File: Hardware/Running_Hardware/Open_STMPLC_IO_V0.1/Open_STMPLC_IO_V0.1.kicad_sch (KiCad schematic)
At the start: 5 parts

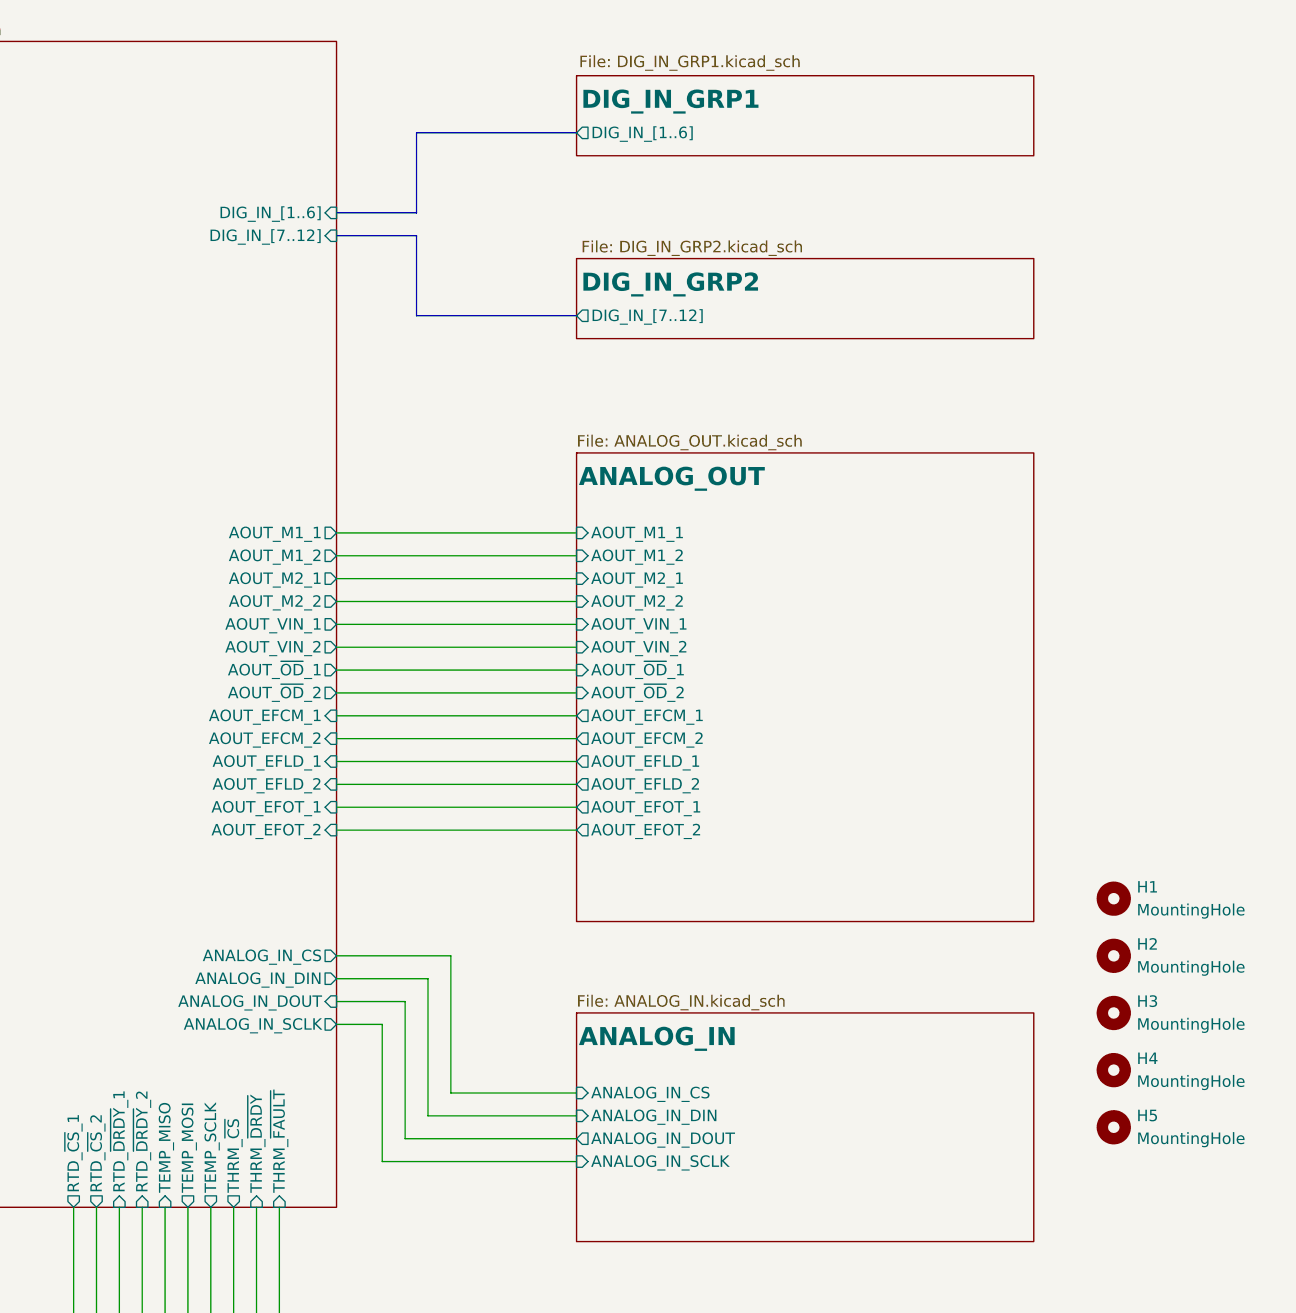
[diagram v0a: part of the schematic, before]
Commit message: Input circuit added
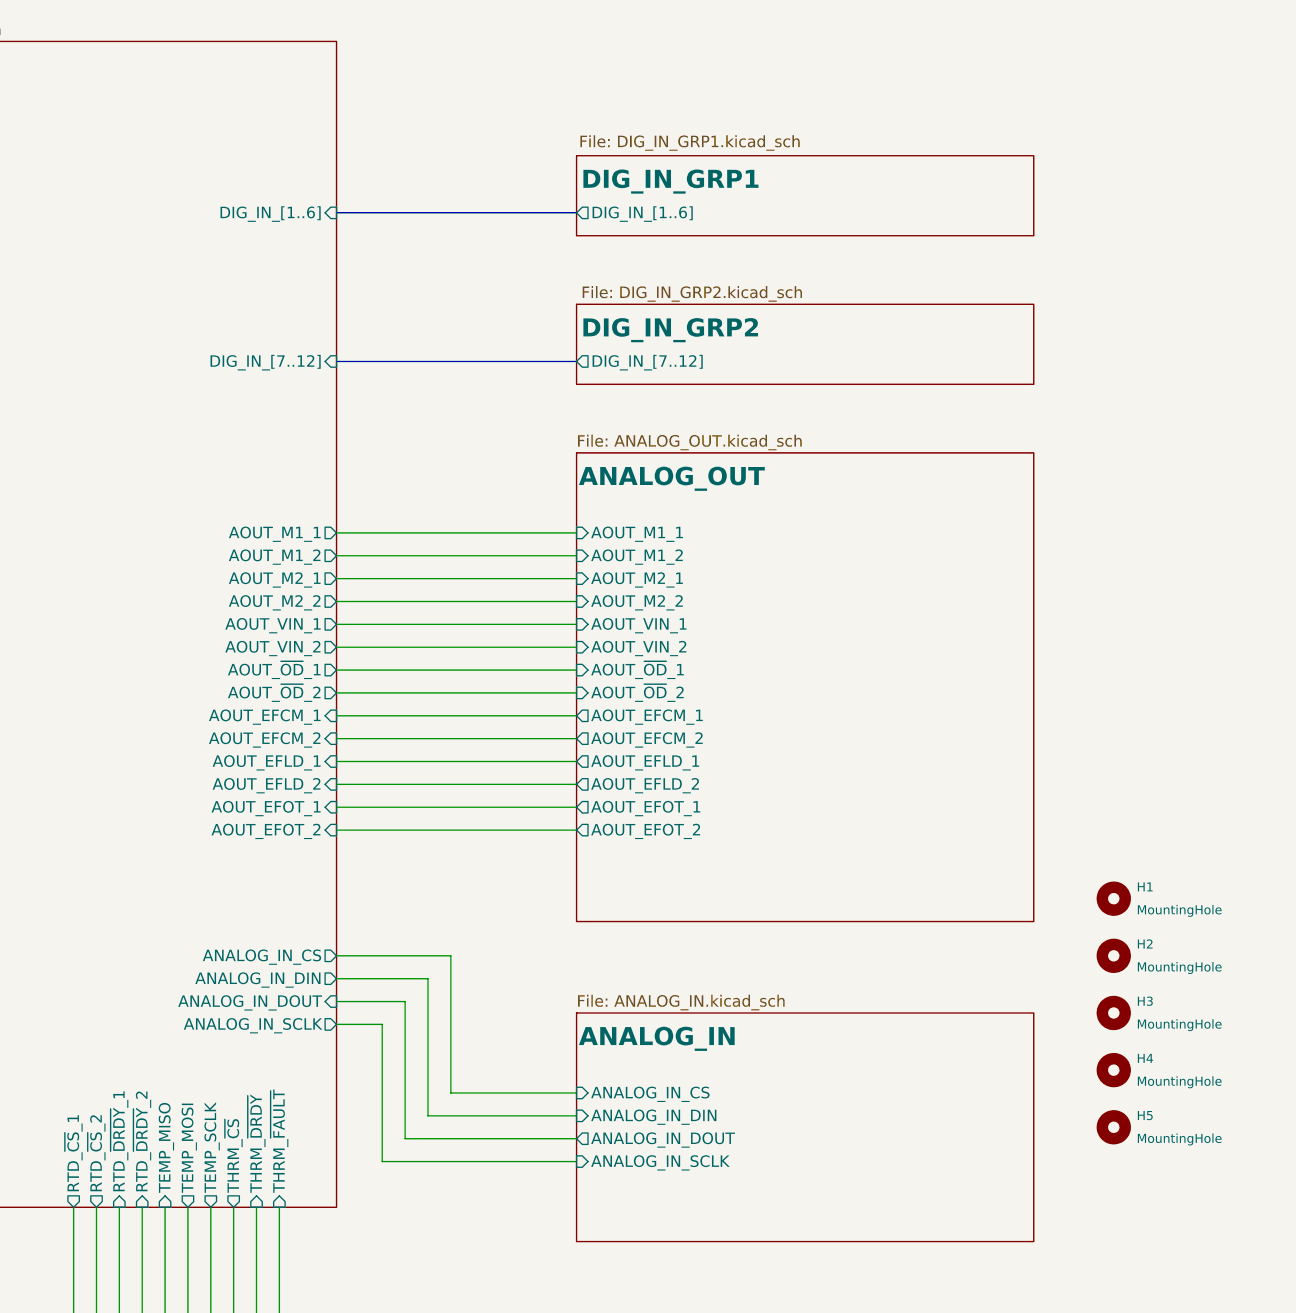
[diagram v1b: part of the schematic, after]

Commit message: IO board layout
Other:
- sheet ANALOG_IN ports: added ANALOG_IN_ERROR; removed none
- sheet B2B_Connector ports: added ANALOG_IN_ERROR; removed none
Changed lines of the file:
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@@
 	(wire
 		(pts
-			(xy 181.61 143.51) (xy 203.2 143.51)
+			(xy 186.69 143.51) (xy 203.2 143.51)
 		)
 		(stroke
@@
 	(wire
 		(pts
-			(xy 176.53 120.65) (xy 189.23 120.65)
-		)
-		(stroke
-			(width 0)
-			(type default)
-		)
-	)
-	(wire
-		(pts
-			(xy 189.23 135.89) (xy 203.2 135.89)
+			(xy 176.53 120.65) (xy 194.31 120.65)
+		)
+		(stroke
+			(width 0)
+			(type default)
+		)
+	)
+	(wire
+		(pts
+			(xy 194.31 135.89) (xy 203.2 135.89)
 		)
 		(stroke
@@
 		)
 	)
+	(wire
+		(pts
+			(xy 184.15 146.05) (xy 184.15 130.81)
+		)
+		(stroke
+			(width 0)
+			(type default)
+		)
+	)
 	(bus
 		(pts
@@
 	(wire
 		(pts
-			(xy 186.69 123.19) (xy 186.69 138.43)
+			(xy 191.77 123.19) (xy 191.77 138.43)
 		)
 		(stroke
@@
 		)
 	)
+	(wire
+		(pts
+			(xy 184.15 130.81) (xy 176.53 130.81)
+		)
+		(stroke
+			(width 0)
+			(type default)
+		)
+	)
 	(bus
 		(pts
@@
 	(wire
 		(pts
-			(xy 176.53 123.19) (xy 186.69 123.19)
+			(xy 176.53 123.19) (xy 191.77 123.19)
 		)
 		(stroke
@@
 	(wire
 		(pts
-			(xy 184.15 140.97) (xy 203.2 140.97)
+			(xy 189.23 140.97) (xy 203.2 140.97)
 		)
 		(stroke
@@
 	(wire
 		(pts
-			(xy 184.15 125.73) (xy 184.15 140.97)
+			(xy 189.23 125.73) (xy 189.23 140.97)
 		)
 		(stroke
@@
 	(wire
 		(pts
-			(xy 176.53 128.27) (xy 181.61 128.27)
+			(xy 176.53 128.27) (xy 186.69 128.27)
 		)
 		(stroke
@@
 	(wire
 		(pts
+			(xy 203.2 146.05) (xy 184.15 146.05)
+		)
+		(stroke
+			(width 0)
+			(type default)
+		)
+	)
+	(wire
+		(pts
 			(xy 68.58 107.95) (xy 113.03 107.95)
 		)
@@
 	(wire
 		(pts
-			(xy 181.61 128.27) (xy 181.61 143.51)
+			(xy 186.69 128.27) (xy 186.69 143.51)
 		)
 		(stroke
@@
 	(wire
 		(pts
-			(xy 176.53 125.73) (xy 184.15 125.73)
+			(xy 176.53 125.73) (xy 189.23 125.73)
 		)
 		(stroke
@@
 	(wire
 		(pts
-			(xy 186.69 138.43) (xy 203.2 138.43)
+			(xy 191.77 138.43) (xy 203.2 138.43)
 		)
 		(stroke
@@
 	(wire
 		(pts
-			(xy 189.23 120.65) (xy 189.23 135.89)
+			(xy 194.31 120.65) (xy 194.31 135.89)
 		)
 		(stroke
@@
 			)
 		)
+		(pin "ANALOG_IN_ERROR" output
+			(at 203.2 146.05 180)
+			(effects
+				(font
+					(size 1.27 1.27)
+				)
+				(justify left)
+			)
+		)
 		(instances
 			(project "Open_STMPLC_IO_V0.1"
@@
 			)
 		)
+		(pin "ANALOG_IN_ERROR" input
+			(at 176.53 130.81 0)
+			(effects
+				(font
+					(size 1.27 1.27)
+				)
+				(justify right)
+			)
+		)

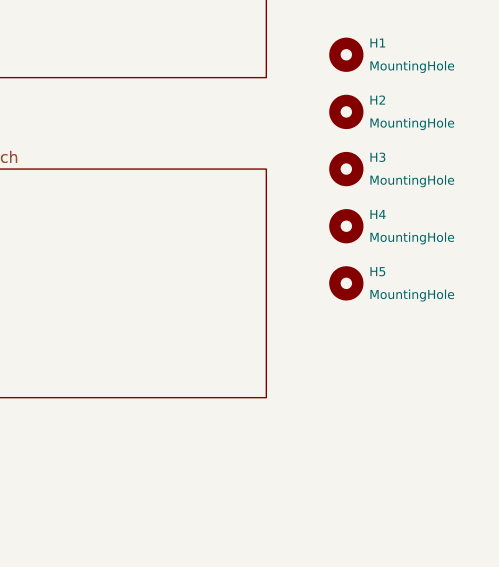
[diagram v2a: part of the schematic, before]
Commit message: Pin mapping IO connector
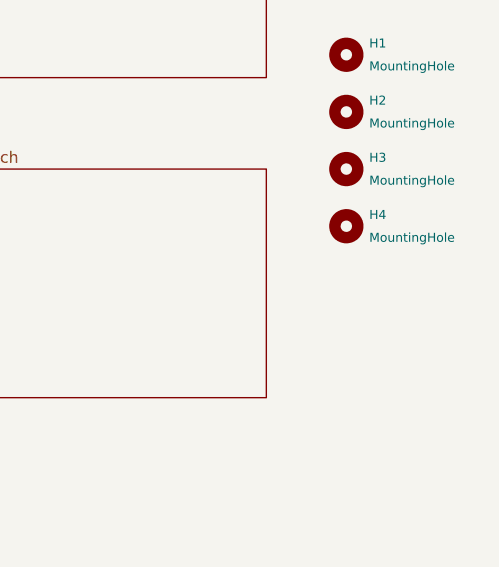
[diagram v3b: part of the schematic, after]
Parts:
- removed H5: MountingHole, MountingHole:MountingHole_3.2mm_M3, symbol Mechanical:MountingHole
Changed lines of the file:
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@@
-		)
-	)
-	(symbol
-		(lib_id "Mechanical:MountingHole")
-		(at 262.89 139.7 0)
-		(unit 1)
-		(exclude_from_sim no)
-		(in_bom no)
-		(on_board yes)
-		(dnp no)
-		(fields_autoplaced yes)
-		(property "Reference" "H5"
-			(at 265.43 138.4299 0)
-			(effects
-				(font
-					(size 1 1)
-				)
-				(justify left)
-			)
-		)
-		(property "Value" "MountingHole"
-			(at 265.43 140.9699 0)
-			(effects
-				(font
-					(size 1 1)
-				)
-				(justify left)
-			)
-		)
-		(property "Footprint" "MountingHole:MountingHole_3.2mm_M3"
-			(at 262.89 139.7 0)
-			(effects
-				(font
-					(size 1.27 1.27)
-				)
-				(hide yes)
-			)
-		)
-		(property "Datasheet" "~"
-			(at 262.89 139.7 0)
-			(effects
-				(font
-					(size 1.27 1.27)
-				)
-				(hide yes)
-			)
-		)
-		(property "Description" "Mounting Hole without connection"
-			(at 262.89 139.7 0)
-			(effects
-				(font
-					(size 1.27 1.27)
-				)
-				(hide yes)
-			)
-		)
-		(instances
-			(project "Open_STMPLC_IO_V0.1"
-				(path "/4d6787b6-1f4f-4098-b70b-d936e584350b"
-					(reference "H5")
-					(unit 1)
-				)
-			)
 		)
 	)

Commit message: IO board layout
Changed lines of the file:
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@@
 		)
 		(pin "DIG_OUT_DIAG_[1..8]" output
-			(at 113.03 137.16 180)
+			(at 113.03 139.7 180)
 			(effects
 				(font
@@
 		)
 		(pin "DIG_OUT_[1..8]" output
-			(at 113.03 139.7 180)
+			(at 113.03 137.16 180)
 			(effects
 				(font

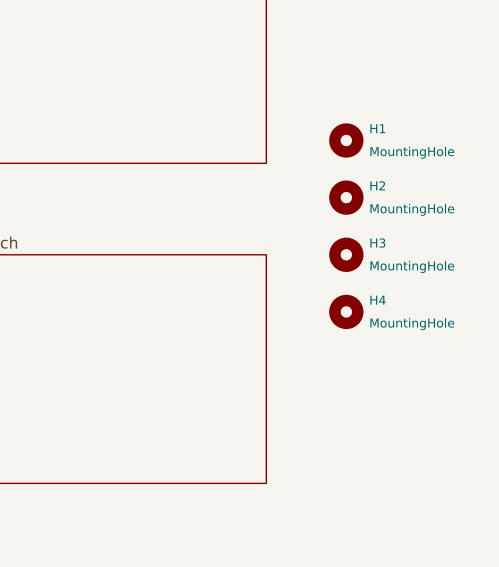
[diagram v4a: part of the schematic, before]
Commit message: IO board layout completion and DRC clear
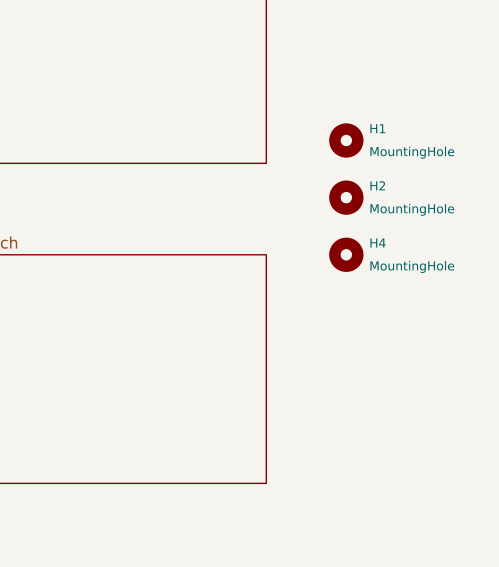
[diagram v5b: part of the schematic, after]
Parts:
- removed H3: MountingHole, MountingHole:MountingHole_3.2mm_M3, symbol Mechanical:MountingHole
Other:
- moved on the sheet: H4
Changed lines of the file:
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@@
 		(dnp no)
 		(fields_autoplaced yes)
-		(property "Reference" "H3"
+		(property "Reference" "H4"
 			(at 265.43 125.7299 0)
 			(effects
@@
 			(effects
 				(font
-					(size 1.27 1.27)
-				)
-				(hide yes)
-			)
-		)
-		(instances
-			(project "Open_STMPLC_IO_V0.1"
-				(path "/4d6787b6-1f4f-4098-b70b-d936e584350b"
-					(reference "H3")
-					(unit 1)
-				)
-			)
-		)
-	)
-	(symbol
-		(lib_id "Mechanical:MountingHole")
-		(at 262.89 133.35 0)
-		(unit 1)
-		(exclude_from_sim no)
-		(in_bom no)
-		(on_board yes)
-		(dnp no)
-		(fields_autoplaced yes)
-		(property "Reference" "H4"
-			(at 265.43 132.0799 0)
-			(effects
-				(font
-					(size 1 1)
-				)
-				(justify left)
-			)
-		)
-		(property "Value" "MountingHole"
-			(at 265.43 134.6199 0)
-			(effects
-				(font
-					(size 1 1)
-				)
-				(justify left)
-			)
-		)
-		(property "Footprint" "MountingHole:MountingHole_3.2mm_M3"
-			(at 262.89 133.35 0)
-			(effects
-				(font
-					(size 1.27 1.27)
-				)
-				(hide yes)
-			)
-		)
-		(property "Datasheet" "~"
-			(at 262.89 133.35 0)
-			(effects
-				(font
-					(size 1.27 1.27)
-				)
-				(hide yes)
-			)
-		)
-		(property "Description" "Mounting Hole without connection"
-			(at 262.89 133.35 0)
-			(effects
-				(font

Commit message: PCB routing completion v0.1 Main
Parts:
- added FID1, FID2, FID3, FID4: Fiducial, Fiducial:Fiducial_1mm_Mask3mm, symbol Mechanical:Fiducial

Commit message: Silkscreen and DRC
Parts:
- added FID5, FID6, FID7, FID8: Fiducial, Fiducial:Fiducial_1mm_Mask3mm, symbol Mechanical:Fiducial
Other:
- moved on the sheet: FID1, FID2, FID3, FID4

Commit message: Gerber generation v0.1
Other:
- company: (none) -> Thingslista Automation LLP
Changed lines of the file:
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@@
 	(title_block
 		(title "Open_STMPLC_IO")
-		(date "2026-05-23")
+		(date "2026-06-03")
 		(rev "0.1")
+		(company "Thingslista Automation LLP")
 	)
 	(wire
